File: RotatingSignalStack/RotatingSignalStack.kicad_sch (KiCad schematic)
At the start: 0 parts

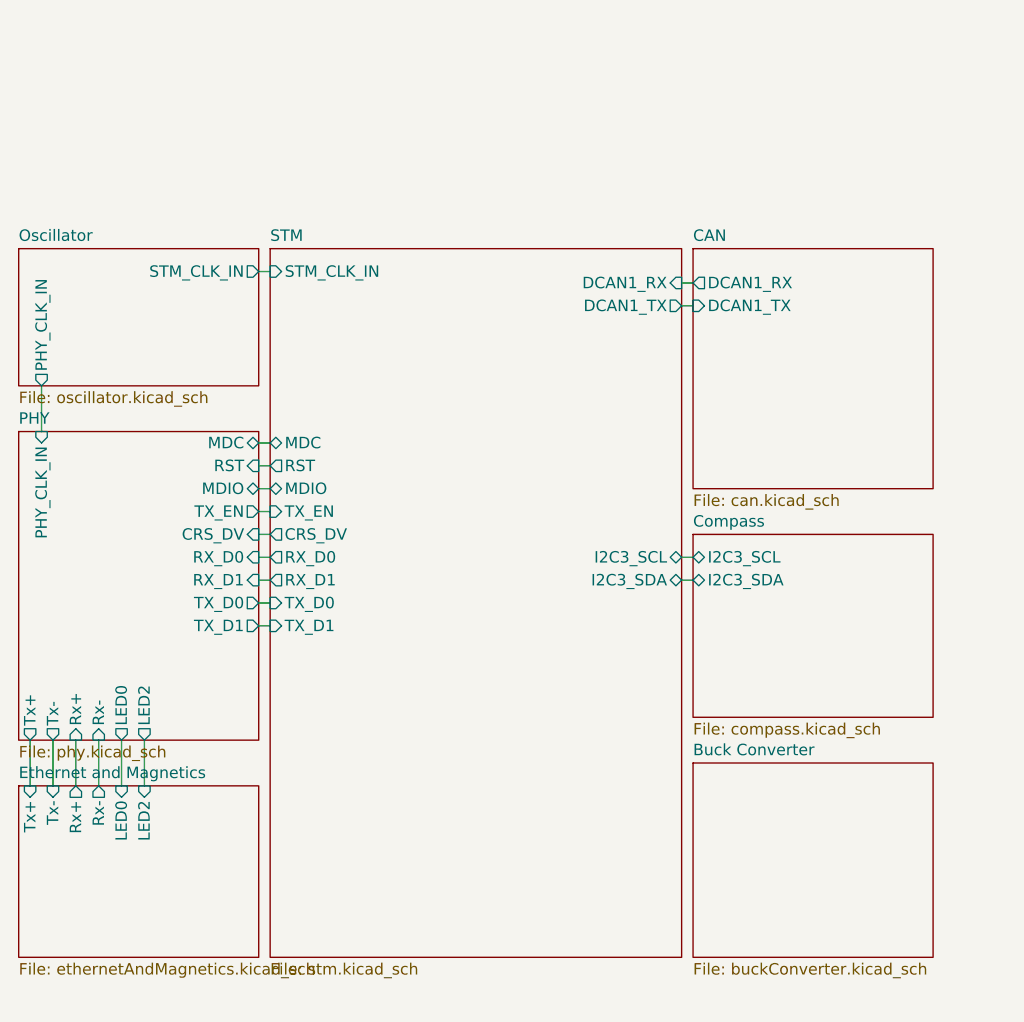
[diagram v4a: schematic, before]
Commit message: BUCK pins
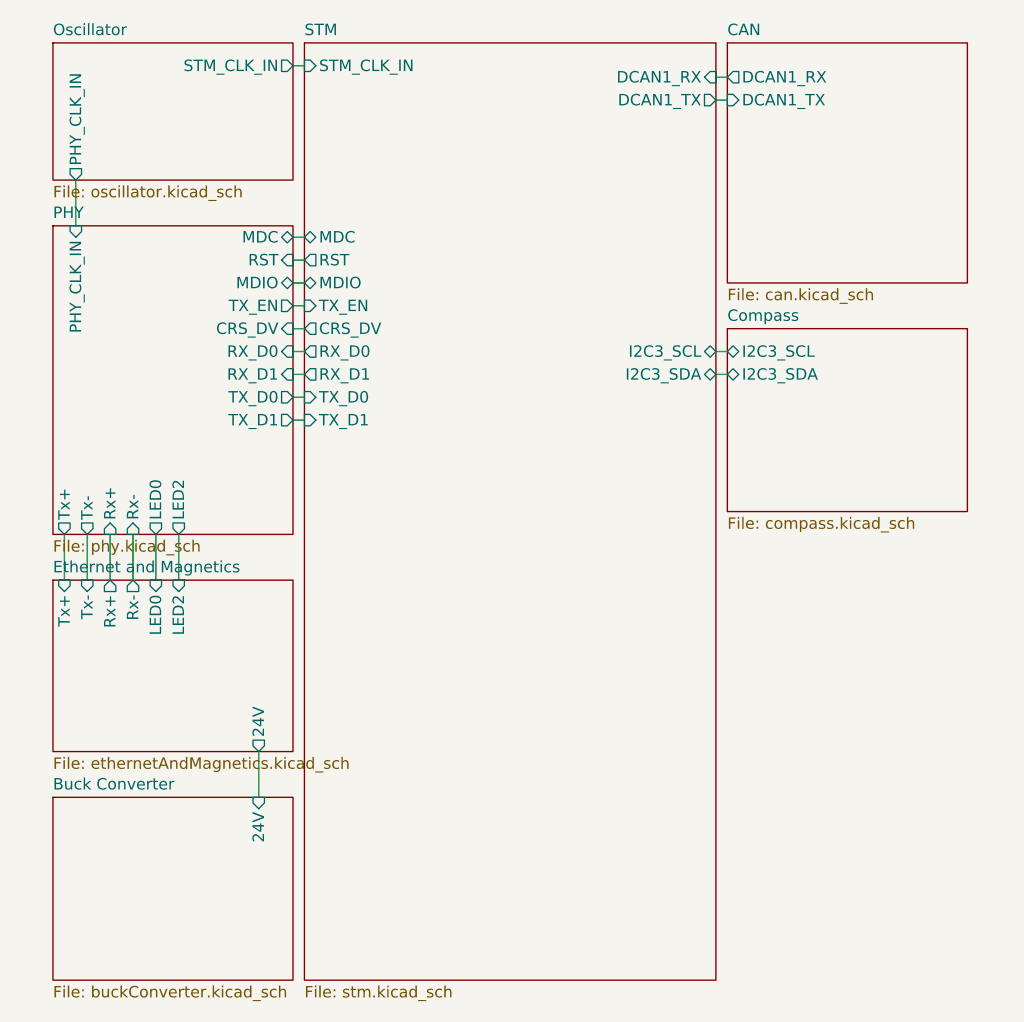
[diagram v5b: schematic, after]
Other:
- sheet Buck Converter ports: added 24V; removed none
- sheet Ethernet and Magnetics ports: added 24V; removed none

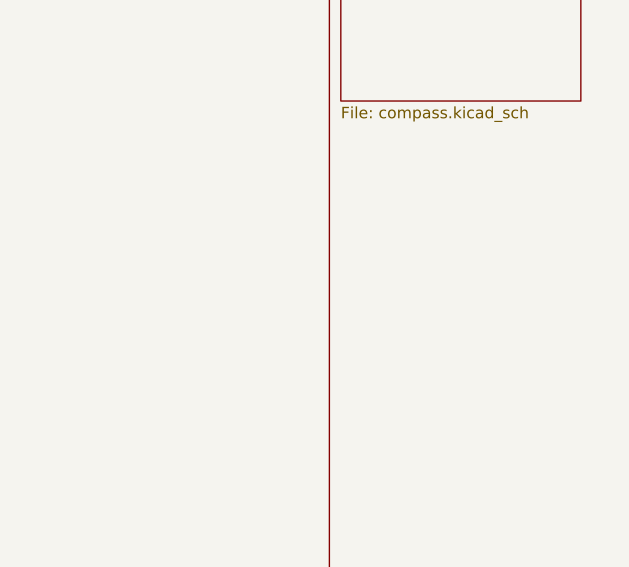
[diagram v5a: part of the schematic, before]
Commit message: Added motor connectors
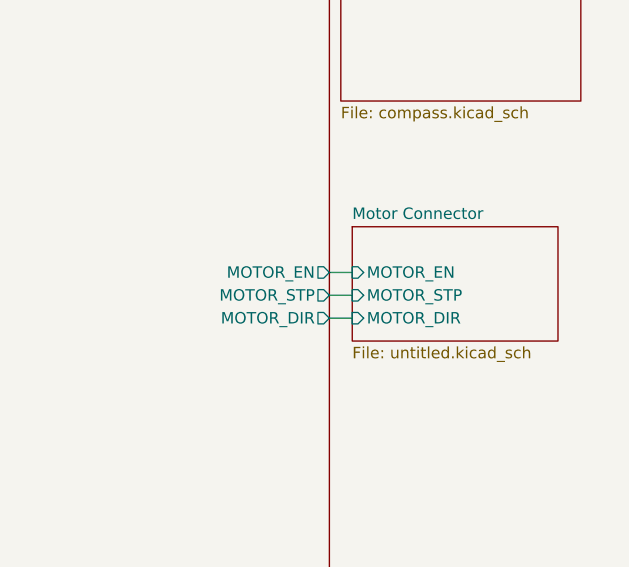
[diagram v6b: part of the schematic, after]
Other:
- added sheet Motor Connector (untitled.kicad_sch)
- sheet STM ports: added MOTOR_DIR, MOTOR_EN, MOTOR_STP; removed none
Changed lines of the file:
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@@
+	(wire
+		(pts
+			(xy 173.99 104.14) (xy 176.53 104.14)
+		)
+		(stroke
+			(width 0)
+			(type default)
+		)
+	)
 	(wire
 		(pts
@@
 	(wire
 		(pts
+			(xy 173.99 106.68) (xy 176.53 106.68)
+		)
+		(stroke
+			(width 0)
+			(type default)
+		)
+	)
+	(wire
+		(pts
 			(xy 123.19 111.76) (xy 123.19 116.84)
 		)
@@
 		(pts
 			(xy 127 72.39) (xy 128.27 72.39)
+		)
+		(stroke
+			(width 0)
+			(type default)
+		)
+	)
+	(wire
+		(pts
+			(xy 173.99 109.22) (xy 176.53 109.22)
 		)
 		(stroke
@@
 			)
 		)
+		(pin "MOTOR_STP" output
+			(at 173.99 106.68 0)
+			(effects
+				(font
+					(size 1.27 1.27)
+				)
+				(justify right)
+			)
+		)
+		(pin "MOTOR_DIR" output
+			(at 173.99 109.22 0)
+			(effects
+				(font
+					(size 1.27 1.27)
+				)
+				(justify right)
+			)
+		)
+		(pin "MOTOR_EN" output
+			(at 173.99 104.14 0)
+			(effects
+				(font
+					(size 1.27 1.27)
+				)
+				(justify right)
+			)
+		)
 		(instances
 			(project "RotatingSignalStack"
@@
 				)
 			)
+		)
+	)
+	(sheet
+		(at 176.53 99.06)
+		(size 22.86 12.7)
+		(exclude_from_sim no)
+		(in_bom yes)
+		(on_board yes)
+		(dnp no)
+		(fields_autoplaced yes)
+		(stroke
+			(width 0.1524)
+			(type solid)
+		)
+		(fill
+			(color 0 0 0 0.0000)
+		)
+		(property "Sheetname" "Motor Connector"
+			(at 176.53 98.3484 0)
+			(effects
+				(font
+					(size 1.27 1.27)
+				)
+				(justify left bottom)
+			)
+		)
+		(property "Sheetfile" "untitled.kicad_sch"
+			(at 176.53 112.3446 0)
+			(effects
+				(font
+					(size 1.27 1.27)
+				)
+				(justify left top)
+			)
+		)
+		(pin "MOTOR_DIR" input
+			(at 176.53 109.22 180)
+			(effects
+				(font
+					(size 1.27 1.27)
+				)
+				(justify left)
+			)
+		)
+		(pin "MOTOR_EN" input
+			(at 176.53 104.14 180)
+			(effects
+				(font
+					(size 1.27 1.27)
+				)
+				(justify left)
+			)
+		)
+		(pin "MOTOR_STP" input
+			(at 176.53 106.68 180)
+			(effects
+				(font
+					(size 1.27 1.27)
+				)
+				(justify left)
+			)
+		)
+		(instances
+			(project "RotatingSignalStack"
+				(path "/fbbbfa89-3c28-4cf8-856b-66ca7308742c"
+					(page "9")
+				)
+			)

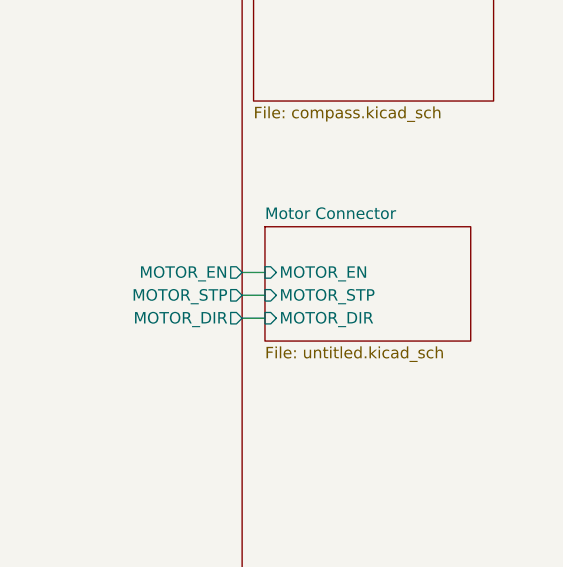
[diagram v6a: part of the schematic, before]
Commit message: Added CAN ESD protection
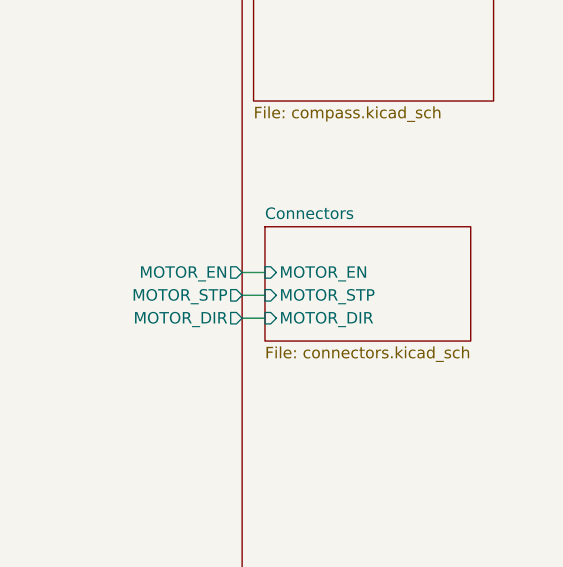
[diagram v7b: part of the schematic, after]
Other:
- sheet Motor Connector renamed Connectors
- sheet Connectors: file untitled.kicad_sch -> connectors.kicad_sch
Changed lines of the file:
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@@
 			(color 0 0 0 0.0000)
 		)
-		(property "Sheetname" "Motor Connector"
+		(property "Sheetname" "Connectors"
 			(at 176.53 98.3484 0)
 			(effects
@@
 			)
 		)
-		(property "Sheetfile" "untitled.kicad_sch"
+		(property "Sheetfile" "connectors.kicad_sch"
 			(at 176.53 112.3446 0)
 			(effects

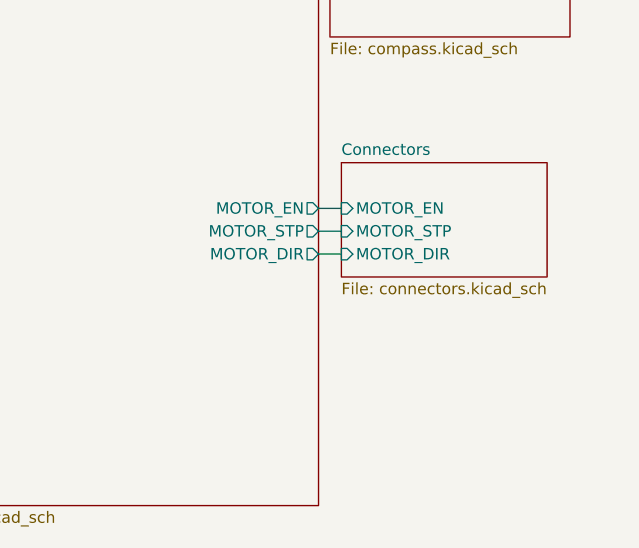
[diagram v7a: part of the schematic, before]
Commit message: Added Compass ESD protection
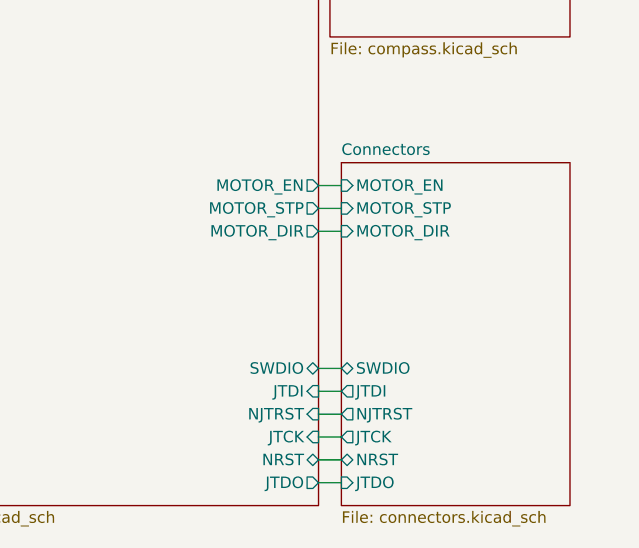
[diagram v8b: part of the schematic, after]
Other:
- sheet Connectors ports: added JTCK, JTDI, JTDO, NJTRST, NRST, SWDIO; removed none
- sheet STM ports: added JTCK, JTDI, JTDO, NJTRST, NRST, SWDIO; removed none
